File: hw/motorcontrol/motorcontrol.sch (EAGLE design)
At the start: 86 parts, among them U1 BTN8982TA, U10 BSS138BKS, U2 BTN8982TA, U3 BTN8982TA, U7 PTR08060W

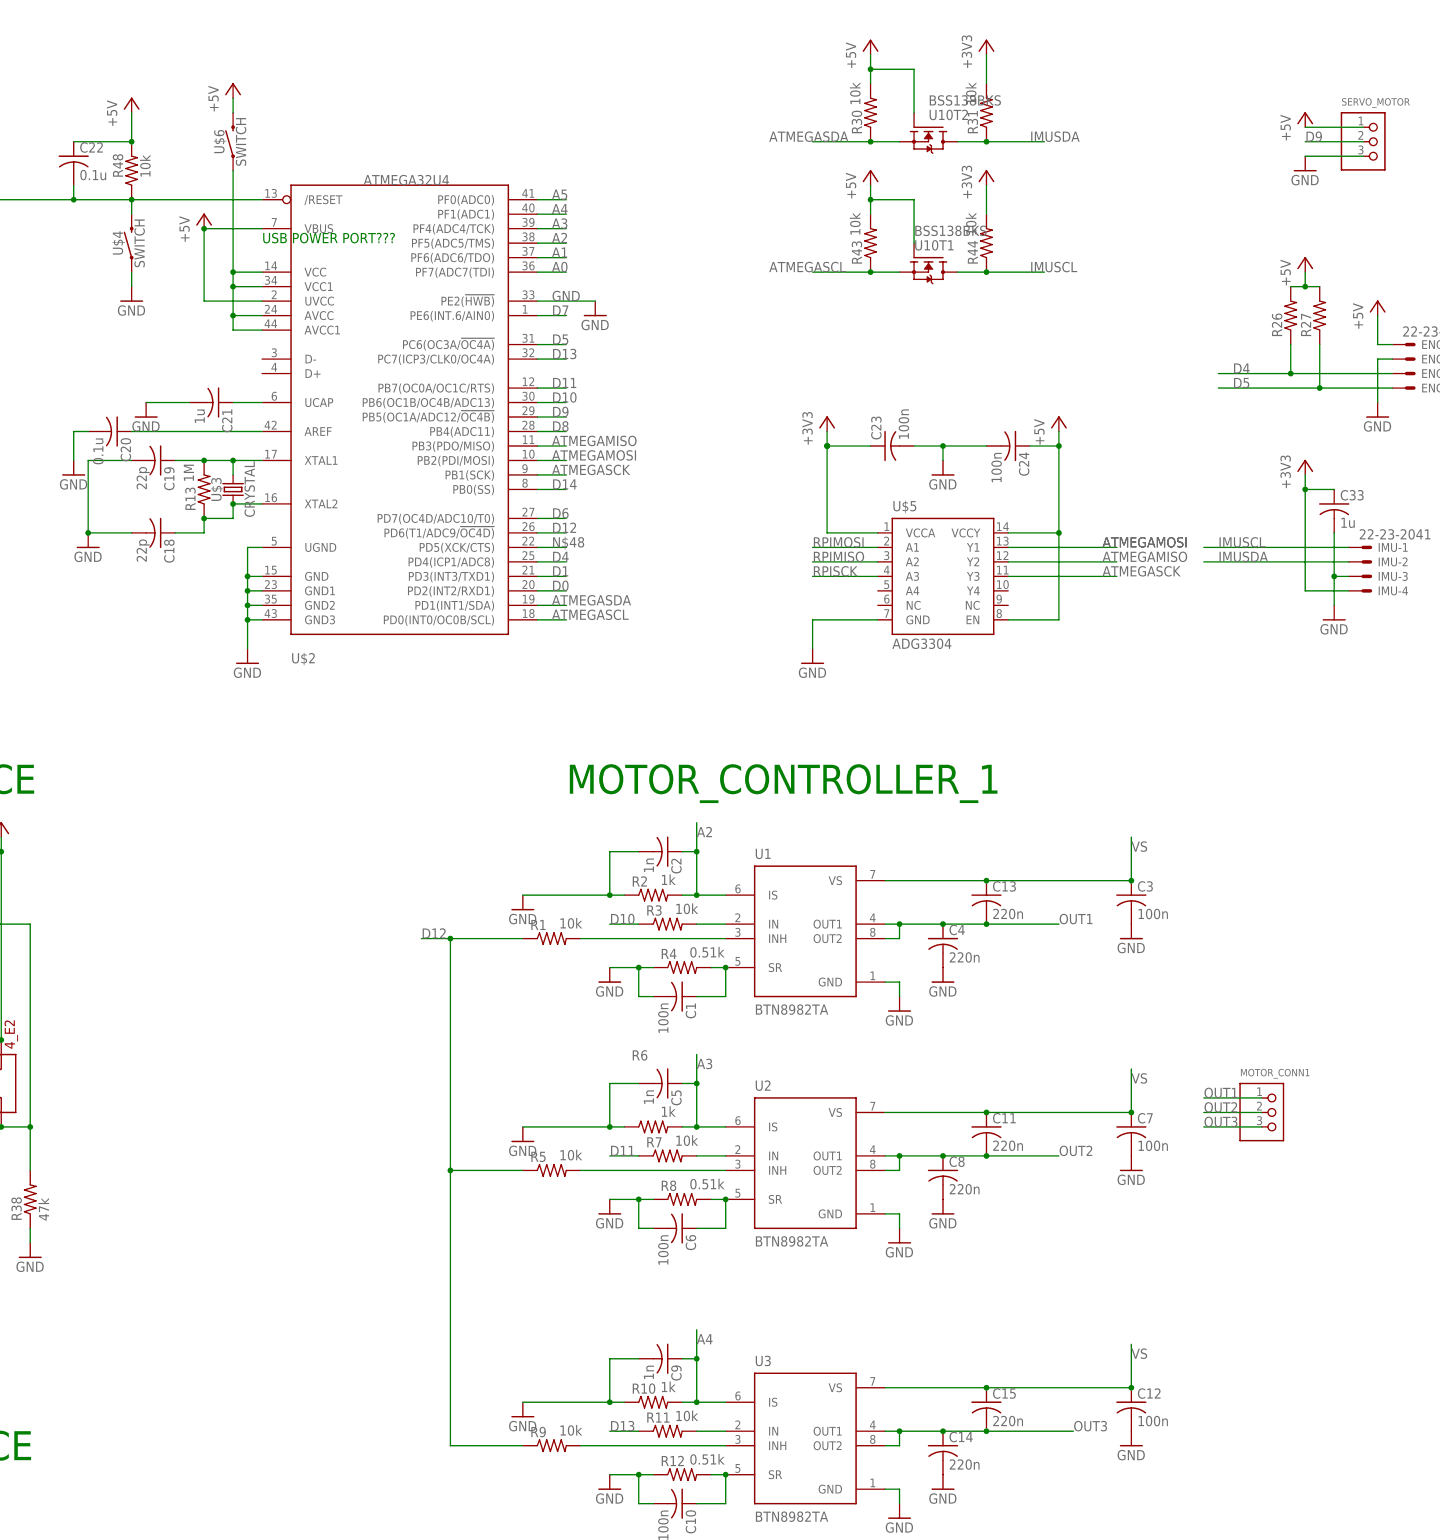
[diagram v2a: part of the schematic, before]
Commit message: Revert "Revert "schematics and parts list""
This reverts commit 970b9175388dfda417d99c9230ef583c3620850f.
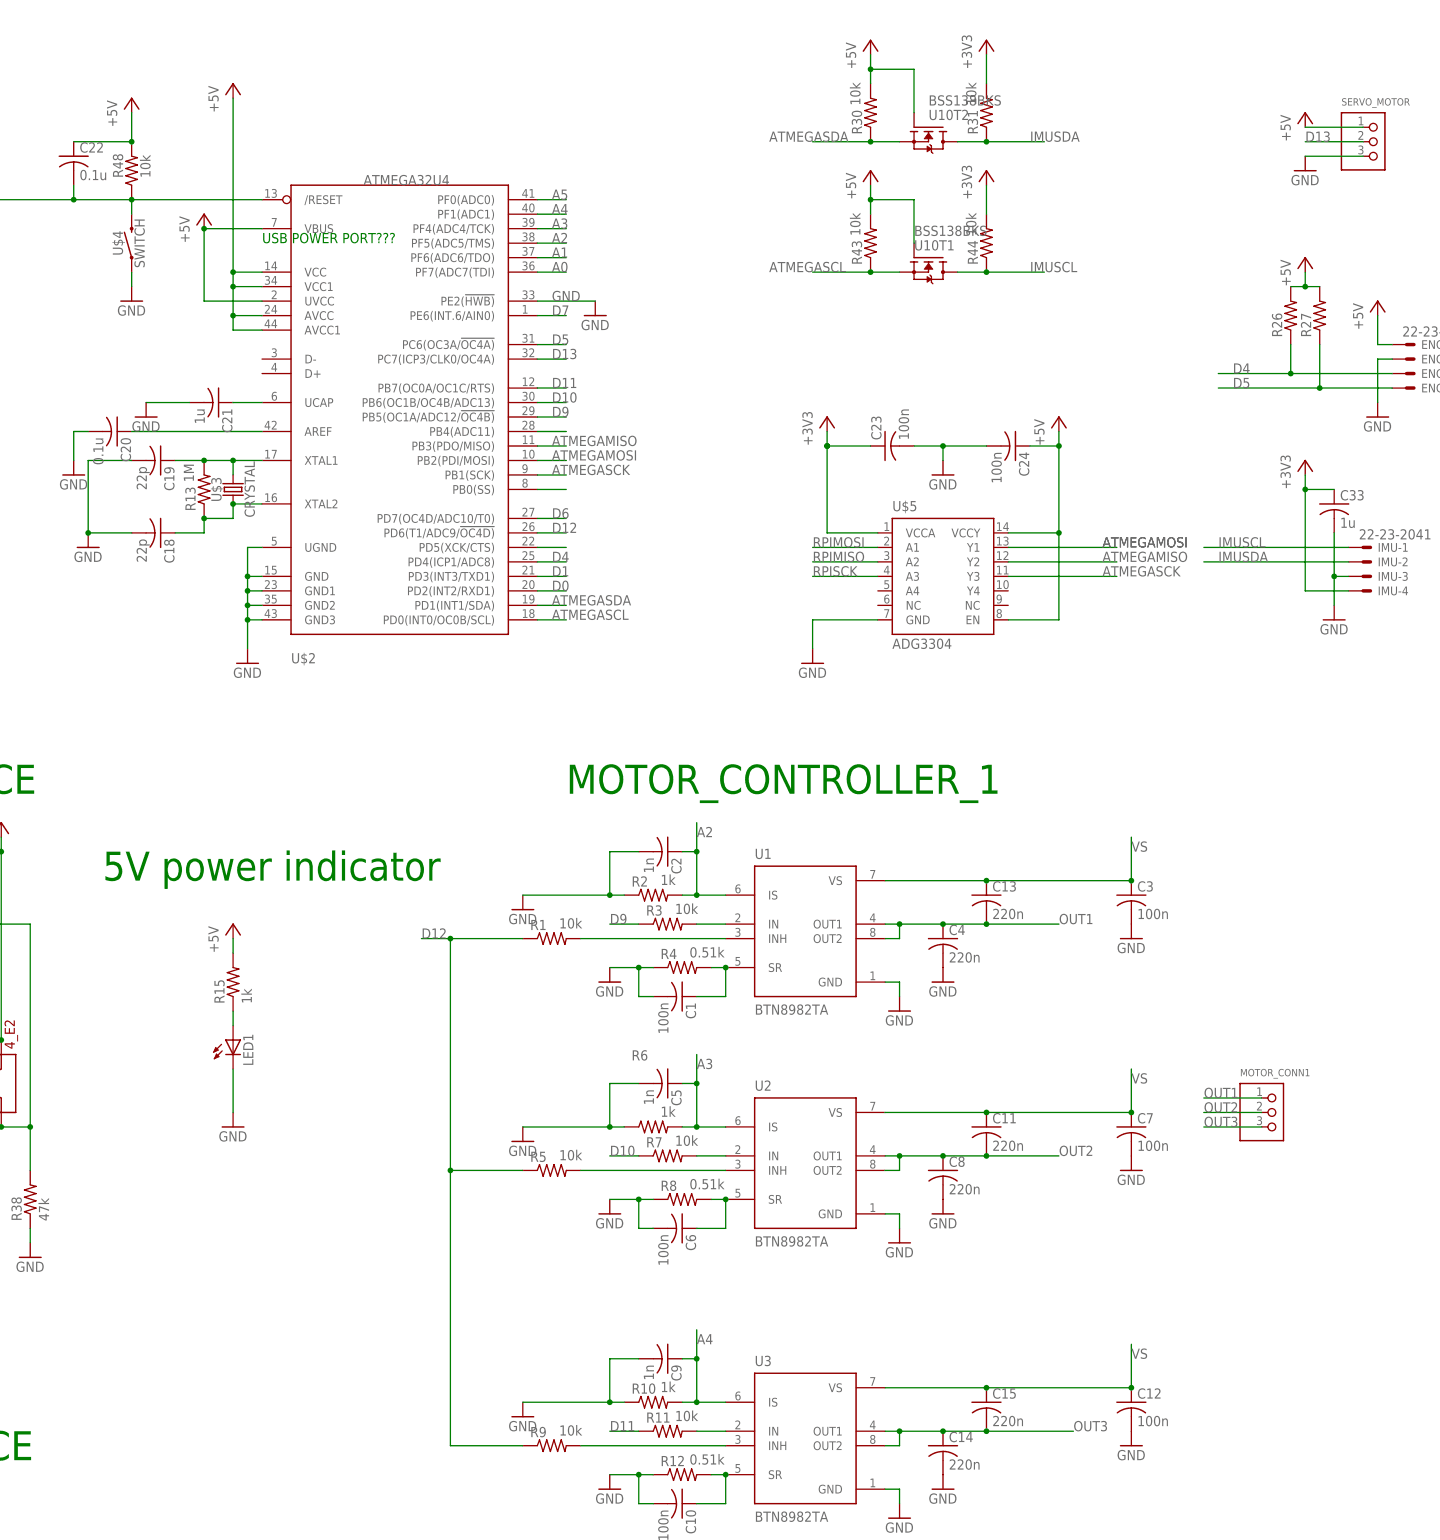
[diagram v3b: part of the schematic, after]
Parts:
- removed U$6: SWITCH, rpibout:SWITCH
- added LED1: (no value), led:LEDSMT1206
- added R15: 1k, resistor:R-US_R1206
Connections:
- removed net N$13: SERVO_MOTOR.P3
- removed net N$14: U$2.AVCC, U$2.AVCC1, U$2.VCC, U$2.VCC1, U$6.1
- new net N$22: LED1.A, R15.1
- net +5V: now also R15.2, U$2.AVCC, U$2.AVCC1, U$2.VCC, U$2.VCC1; no longer U$6.2
- net D10: now also R7.1; no longer R3.1
- net D11: now also R11.1; no longer R7.1
- net D13: now also SERVO_MOTOR.P2; no longer R11.1
- net D9: now also R3.1; no longer SERVO_MOTOR.P2
- net GND: now also LED1.C, SERVO_MOTOR.P3
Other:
- note added: "5V power indicator"
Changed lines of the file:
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@@
 <layer number="19" name="Unrouted" color="6" fill="1" visible="no" active="no"/>
 <layer number="20" name="Dimension" color="15" fill="1" visible="no" active="no"/>
-<layer number="21" name="tPlace" color="14" fill="1" visible="no" active="no"/>
+<layer number="21" name="tPlace" color="7" fill="1" visible="no" active="no"/>
 <layer number="22" name="bPlace" color="7" fill="1" visible="no" active="no"/>
-<layer number="23" name="tOrigins" color="10" fill="1" visible="no" active="no"/>
+<layer number="23" name="tOrigins" color="15" fill="1" visible="no" active="no"/>
 <layer number="24" name="bOrigins" color="15" fill="1" visible="no" active="no"/>
 <layer number="25" name="tNames" color="7" fill="1" visible="no" active="no"/>
@@
 <layer number="37" name="tTest" color="7" fill="1" visible="no" active="no"/>
 <layer number="38" name="bTest" color="7" fill="1" visible="no" active="no"/>
-<layer number="39" name="tKeepout" color="2" fill="11" visible="no" active="no"/>
+<layer number="39" name="tKeepout" color="4" fill="11" visible="no" active="no"/>
 <layer number="40" name="bKeepout" color="1" fill="11" visible="no" active="no"/>
 <layer number="41" name="tRestrict" color="4" fill="10" visible="no" active="no"/>
@@
 <layer number="46" name="Milling" color="3" fill="1" visible="no" active="no"/>
 <layer number="47" name="Measures" color="7" fill="1" visible="no" active="no"/>
-<layer number="48" name="Document" color="13" fill="1" visible="no" active="no"/>
+<layer number="48" name="Document" color="7" fill="1" visible="no" active="no"/>
 <layer number="49" name="Reference" color="7" fill="1" visible="no" active="no"/>
 <layer number="50" name="dxf" color="7" fill="1" visible="no" active="no"/>
@@
 <part name="GND25" library="supply1" deviceset="GND" device=""/>
 <part name="GND26" library="supply1" deviceset="GND" device=""/>
-<part name="U$6" library="rpibout" deviceset="SWITCH" device=""/>
 <part name="P+6" library="supply1" deviceset="+5V" device=""/>
+<part name="LED1" library="led" deviceset="LED" device="SMT1206"/>
+<part name="P+10" library="supply1" deviceset="+5V" device=""/>
+<part name="GND27" library="supply1" deviceset="GND" device=""/>
+<part name="R15" library="resistor" deviceset="R-US_" device="R1206" value="1k"/>
 </parts>
 <sheets>
@@
 <text x="-78.74" y="170.18" size="5.08" layer="91">Raspberry Pi GPIO</text>
 <text x="30.48" y="137.16" size="1.778" layer="91">USB POWER PORT???</text>
+<text x="2.54" y="25.4" size="5.08" layer="91">5V power indicator</text>
 </plain>
 <instances>
@@
 <instance part="GND25" gate="1" x="127" y="63.5"/>
 <instance part="GND26" gate="1" x="149.86" y="96.52"/>
-<instance part="U$6" gate="G$1" x="25.4" y="154.94" rot="R90"/>
 <instance part="P+6" gate="1" x="25.4" y="165.1"/>
+<instance part="LED1" gate="G$1" x="25.4" y="-2.54"/>
+<instance part="P+10" gate="1" x="25.4" y="17.78"/>
+<instance part="GND27" gate="1" x="25.4" y="-17.78"/>
+<instance part="R15" gate="G$1" x="25.4" y="7.62" rot="R90"/>
 </instances>
 <busses>
@@
 <wire x1="157.48" y1="101.6" x2="149.86" y2="101.6" width="0.1524" layer="91"/>
 <junction x="149.86" y="101.6"/>
+</segment>
+<segment>
+<pinref part="LED1" gate="G$1" pin="C"/>
+<pinref part="GND27" gate="1" pin="GND"/>
+<wire x1="25.4" y1="-7.62" x2="25.4" y2="-15.24" width="0.1524" layer="91"/>
+</segment>
+<segment>
+<pinref part="SERVO_MOTOR" gate="G$1" pin="P3"/>
+<wire x1="223.52" y1="152.4" x2="213.36" y2="152.4" width="0.1524" layer="91"/>
+<pinref part="GND16" gate="1" pin="GND"/>
 </segment>
 </net>
@@
 </segment>
 <segment>
-<pinref part="U$6" gate="G$1" pin="2"/>
+<pinref part="P+10" gate="1" pin="+5V"/>
+<pinref part="R15" gate="G$1" pin="2"/>
+<wire x1="25.4" y1="15.24" x2="25.4" y2="12.7" width="0.1524" layer="91"/>
+</segment>
+<segment>
+<pinref part="U$2" gate="G$1" pin="VCC"/>
+<wire x1="30.48" y1="132.08" x2="25.4" y2="132.08" width="0.1524" layer="91"/>
+<pinref part="U$2" gate="G$1" pin="VCC1"/>
+<wire x1="30.48" y1="129.54" x2="25.4" y2="129.54" width="0.1524" layer="91"/>
+<wire x1="25.4" y1="129.54" x2="25.4" y2="132.08" width="0.1524" layer="91"/>
+<pinref part="U$2" gate="G$1" pin="AVCC"/>
+<wire x1="30.48" y1="124.46" x2="25.4" y2="124.46" width="0.1524" layer="91"/>
+<wire x1="25.4" y1="124.46" x2="25.4" y2="129.54" width="0.1524" layer="91"/>
+<junction x="25.4" y="129.54"/>
+<pinref part="U$2" gate="G$1" pin="AVCC1"/>
+<wire x1="30.48" y1="121.92" x2="25.4" y2="121.92" width="0.1524" layer="91"/>
+<wire x1="25.4" y1="121.92" x2="25.4" y2="124.46" width="0.1524" layer="91"/>
+<junction x="25.4" y="124.46"/>
 <pinref part="P+6" gate="1" pin="+5V"/>
-<wire x1="25.4" y1="162.56" x2="25.4" y2="160.02" width="0.1524" layer="91"/>
+<wire x1="25.4" y1="162.56" x2="25.4" y2="132.08" width="0.1524" layer="91"/>
+<junction x="25.4" y="132.08"/>
 </segment>
 </net>
@@
 </segment>
 <segment>
+<pinref part="SERVO_MOTOR" gate="G$1" pin="P2"/>
+<wire x1="213.36" y1="154.94" x2="223.52" y2="154.94" width="0.1524" layer="91"/>
+<label x="213.36" y="154.94" size="1.778" layer="95"/>
+</segment>
+</net>
+<net name="D11" class="0">
+<segment>
+<pinref part="U$2" gate="G$1" pin="PB7(OC0A/OC1C/RTS)"/>
+<wire x1="78.74" y1="111.76" x2="83.82" y2="111.76" width="0.1524" layer="91"/>
+<label x="81.28" y="111.76" size="1.778" layer="95"/>
+</segment>
+<segment>
 <pinref part="R11" gate="G$1" pin="1"/>
 <wire x1="96.52" y1="-71.12" x2="91.44" y2="-71.12" width="0.1524" layer="91"/>
@@
 </segment>
 </net>
-<net name="D11" class="0">
-<segment>
-<pinref part="U$2" gate="G$1" pin="PB7(OC0A/OC1C/RTS)"/>
-<wire x1="78.74" y1="111.76" x2="83.82" y2="111.76" width="0.1524" layer="91"/>
-<label x="81.28" y="111.76" size="1.778" layer="95"/>
+<net name="D10" class="0">
+<segment>
+<pinref part="U$2" gate="G$1" pin="PB6(OC1B/OC4B/ADC13)"/>
+<wire x1="78.74" y1="109.22" x2="83.82" y2="109.22" width="0.1524" layer="91"/>
+<label x="81.28" y="109.22" size="1.778" layer="95"/>
 </segment>
 <segment>
@@
 </segment>
 </net>
-<net name="D10" class="0">
-<segment>
-<pinref part="U$2" gate="G$1" pin="PB6(OC1B/OC4B/ADC13)"/>
-<wire x1="78.74" y1="109.22" x2="83.82" y2="109.22" width="0.1524" layer="91"/>
-<label x="81.28" y="109.22" size="1.778" layer="95"/>
+<net name="D9" class="0">
+<segment>
+<pinref part="U$2" gate="G$1" pin="PB5(OC1A/ADC12/!OC4B)"/>
+<wire x1="78.74" y1="106.68" x2="83.82" y2="106.68" width="0.1524" layer="91"/>
+<label x="81.28" y="106.68" size="1.778" layer="95"/>
 </segment>
 <segment>
@@
 </segment>
 </net>
-<net name="D9" class="0">
-<segment>
-<pinref part="U$2" gate="G$1" pin="PB5(OC1A/ADC12/!OC4B)"/>
-<wire x1="78.74" y1="106.68" x2="83.82" y2="106.68" width="0.1524" layer="91"/>
-<label x="81.28" y="106.68" size="1.778" layer="95"/>
-</segment>
-<segment>
-<pinref part="SERVO_MOTOR" gate="G$1" pin="P2"/>
-<wire x1="213.36" y1="154.94" x2="223.52" y2="154.94" width="0.1524" layer="91"/>
-<label x="213.36" y="154.94" size="1.778" layer="95"/>
-</segment>
-</net>
 <net name="D8" class="0">
 <segment>
 <pinref part="U$2" gate="G$1" pin="PB4(ADC11)"/>
 <wire x1="78.74" y1="104.14" x2="83.82" y2="104.14" width="0.1524" layer="91"/>
-<label x="81.28" y="104.14" size="1.778" layer="95"/>
 </segment>
 </net>
@@
 <pinref part="U$2" gate="G$1" pin="PB0(SS)"/>
 <wire x1="78.74" y1="93.98" x2="83.82" y2="93.98" width="0.1524" layer="91"/>
-<label x="81.28" y="93.98" size="1.778" layer="95"/>
 </segment>
 </net>
@@
 <pinref part="U$2" gate="G$1" pin="PD5(XCK/CTS)"/>
 <wire x1="78.74" y1="83.82" x2="83.82" y2="83.82" width="0.1524" layer="91"/>
-<label x="81.28" y="83.82" size="1.778" layer="95"/>
 </segment>
 </net>
@@
 <label x="177.8" y="83.82" size="1.778" layer="95"/>
 <label x="177.8" y="83.82" size="1.778" layer="95"/>
-</segment>
-</net>
-<net name="N$13" class="0">
-<segment>
-<pinref part="SERVO_MOTOR" gate="G$1" pin="P3"/>
-<wire x1="223.52" y1="152.4" x2="213.36" y2="152.4" width="0.1524" layer="91"/>
-<pinref part="GND16" gate="1" pin="GND"/>
 </segment>
 </net>
@@
 <wire x1="152.4" y1="132.08" x2="157.48" y2="132.08" width="0.1524" layer="91"/>
 <pinref part="R44" gate="G$1" pin="1"/>
-<junction x="157.48" y="132.08"/>
 <wire x1="157.48" y1="132.08" x2="167.64" y2="132.08" width="0.1524" layer="91"/>
 <label x="165.1" y="132.08" size="1.778" layer="95"/>
 <pinref part="U10" gate="T1" pin="D"/>
+<junction x="157.48" y="132.08"/>
 </segment>
 </net>
@@
 </segment>
 </net>
-<net name="N$14" class="0">
-<segment>
-<pinref part="U$2" gate="G$1" pin="VCC"/>
-<wire x1="30.48" y1="132.08" x2="25.4" y2="132.08" width="0.1524" layer="91"/>
-<wire x1="25.4" y1="132.08" x2="25.4" y2="149.86" width="0.1524" layer="91"/>
-<pinref part="U$2" gate="G$1" pin="VCC1"/>
-<wire x1="30.48" y1="129.54" x2="25.4" y2="129.54" width="0.1524" layer="91"/>
-<wire x1="25.4" y1="129.54" x2="25.4" y2="132.08" width="0.1524" layer="91"/>
-<junction x="25.4" y="132.08"/>
-<pinref part="U$2" gate="G$1" pin="AVCC"/>
-<wire x1="30.48" y1="124.46" x2="25.4" y2="124.46" width="0.1524" layer="91"/>
-<wire x1="25.4" y1="124.46" x2="25.4" y2="129.54" width="0.1524" layer="91"/>
-<junction x="25.4" y="129.54"/>
-<pinref part="U$2" gate="G$1" pin="AVCC1"/>
-<wire x1="30.48" y1="121.92" x2="25.4" y2="121.92" width="0.1524" layer="91"/>
-<wire x1="25.4" y1="121.92" x2="25.4" y2="124.46" width="0.1524" layer="91"/>
-<junction x="25.4" y="124.46"/>
-<pinref part="U$6" gate="G$1" pin="1"/>
-</segment>
-</net>
+<net name="N$22" class="0">
+<segment>
+<pinref part="R15" gate="G$1" pin="1"/>
+<pinref part="LED1" gate="G$1" pin="A"/>
+<wire x1="25.4" y1="2.54" x2="25.4" y2="0" width="0.1524" layer="91"/>
+</segment>
+</net>

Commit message: schematics
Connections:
- removed net RPISCLK: J2.23
- net RPISCK: now also J2.23
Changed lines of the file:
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@@
-</segment>
-</net>
-<net name="RPISCLK" class="0">
-<segment>
-<wire x1="-35.56" y1="129.54" x2="-53.34" y2="129.54" width="0.1524" layer="91"/>
-<label x="-53.34" y="129.54" size="1.778" layer="95"/>
-<pinref part="J2" gate="A" pin="23"/>
 </segment>
 </net>
@@
 <label x="127" y="78.74" size="1.778" layer="95"/>
 </segment>
-</net>
-<net name="N$2" class="0">
-<segment>
-<junction x="129.54" y="101.6"/>
-</segment>
-</net>
+<segment>
+<wire x1="-35.56" y1="129.54" x2="-53.34" y2="129.54" width="0.1524" layer="91"/>
+<label x="-53.34" y="129.54" size="1.778" layer="95"/>
+<pinref part="J2" gate="A" pin="23"/>
+</segment>
+</net>

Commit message: backup
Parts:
- removed DMG2305: DMG2305UX, rpibout:DMG2305UX
- removed EEPROM: EEPROM_CAT24C32WI-GT3, rpibout:EEPROM_CAT24C32WI-GT3
- removed JUMPER: 02JUMPER, rpibout:02JUMPER
- removed MMDT5401: MMDT5401, rpibout:MMDT5401
- removed U$1: IPD90P03P4L_04, rpibout:IPD90P03P4L_04
- removed U$5: ADG3304, rpibout:ADG3304
- added J1: (no value), pinhead:PINHD-1X2
- added U11: DMG2305UX, rpibout:DMG2305UX
- added U4: CAT24C32WI-GT3, rpibout:CAT24C32WI-GT3
- added U5: ADG3304, rpibout:ADG3304
- added U6: MMDT5401, rpibout:MMDT5401
- added U8: IPD90P03P4L_04, rpibout:IPD90P03P4L_04
- R15: value 1k -> 10k
- renumbered U$2 to U9
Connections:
- net N$8 renamed RPIRESET
- removed net N$10: EEPROM.SDA, J2.27, R45.1
- removed net N$42: DMG2305.G, MMDT5401.C1, R38.2
- removed net N$43: MMDT5401.B1, MMDT5401.B2, MMDT5401.C2, R37.2
- removed net N$7: EEPROM.SCL, J2.28, R46.1
- removed net VS: C11.1, C12.1, C13.1, C15.1, C16.+, C3.1, C7.1, D1.C, D2.C, U$1.S, U1.VS, U2.VS, U3.VS
- new net N$13: R37.2, U6G$1.B, U6G$1.C, U6G$2.B
- new net N$2: R38.2, U11.G, U6G$2.C
- new net RPISCL: J2.28, R46.1, U4.SCL
- new net RPISDA: J2.27, R45.1, U4.SDA
- new net VPP: C11.1, C12.1, C13.1, C15.1, C16.+, C3.1, C7.1, D1.C, D2.C, U1.VS, U2.VS, U3.VS, U8.S
- net +3V3: now also U4.VCC, U5.VCCA; no longer EEPROM.VCC, U$5.VCCA
- net +5V: now also U11.S, U5.EN, U5.VCCY, U6G$2.E; no longer DMG2305.S, MMDT5401.E1, U$5.EN, U$5.VCCY
- net ATMEGAMISO: now also U5.Y2; no longer U$5.Y2
- net ATMEGAMOSI: now also U5.Y1; no longer U$5.Y1
- net ATMEGASCK: now also U5.Y3; no longer U$5.Y3
- net GND: now also J1.2, U4.A0, U4.A1, U4.A2, U4.VSS, U5.GND; no longer EEPROM.A0, EEPROM.A1, EEPROM.A2, EEPROM.VSS, JUMPER.P1, U$5.GND
- net N$12: now also J1.1, U4.WP; no longer EEPROM.WP, JUMPER.P2
- net N$21: now also U8.G; no longer U$1.G
- net RPIMISO: now also U5.A2; no longer U$5.A2
- net RPIMOSI: now also U5.A1; no longer U$5.A1
- net RPISCK: now also U5.A3; no longer U$5.A3
- net VBATT: now also U8.D; no longer U$1.D
- net VOUT: now also U11.D, U6G$1.E; no longer DMG2305.D, MMDT5401.E2
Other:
- note added: "5V Voltage Regulator and Backpower Protection"
- note added: "Motor Backpower Protection"
- note added: "Motor Controller"
- note added: "Raspberry Pi Hat EEPROM"
- note removed: "5V power indicator"
- note removed: "ARDUINO/RPI POWER SOURCE"
- note removed: "MOTOR_CONTROLLER POWER SOURCE"
- note removed: "MOTOR_CONTROLLER_1"
- moved on the sheet: BATT1, C1, C10, C11, C12, C13, C14, C15, C16, C17, C18, C19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
